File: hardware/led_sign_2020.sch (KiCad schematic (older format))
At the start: 25 parts, among them U1 ESP32-DevKitC, U2 MC74VHC1GT125, U3 MC74VHC1GT125, U4 MAX17601, U5 MAX17601, U6 MAX17601, U7 MAX17601

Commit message: change enable lines to be pulled down and microcontrolled. light up when enabled.
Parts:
- removed R2, R3, R4, R5, R6, R7: 10k, symbol Device:R_Small_US
- added D? (x2): LED, LED_SMD:LED_0805_2012Metric, symbol Device:LED
- added R?: 68ohm, Resistor_SMD:R_0805_2012Metric, symbol Device:R_Small_US
- added R?: 10k, Resistor_SMD:R_0805_2012Metric, symbol Device:R_Small_US
- R1: value 10k -> 4.7k; footprint (none) -> Resistor_SMD:R_0805_2012Metric
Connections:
- wire segments 188 -> 176
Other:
- moved on the sheet: R1

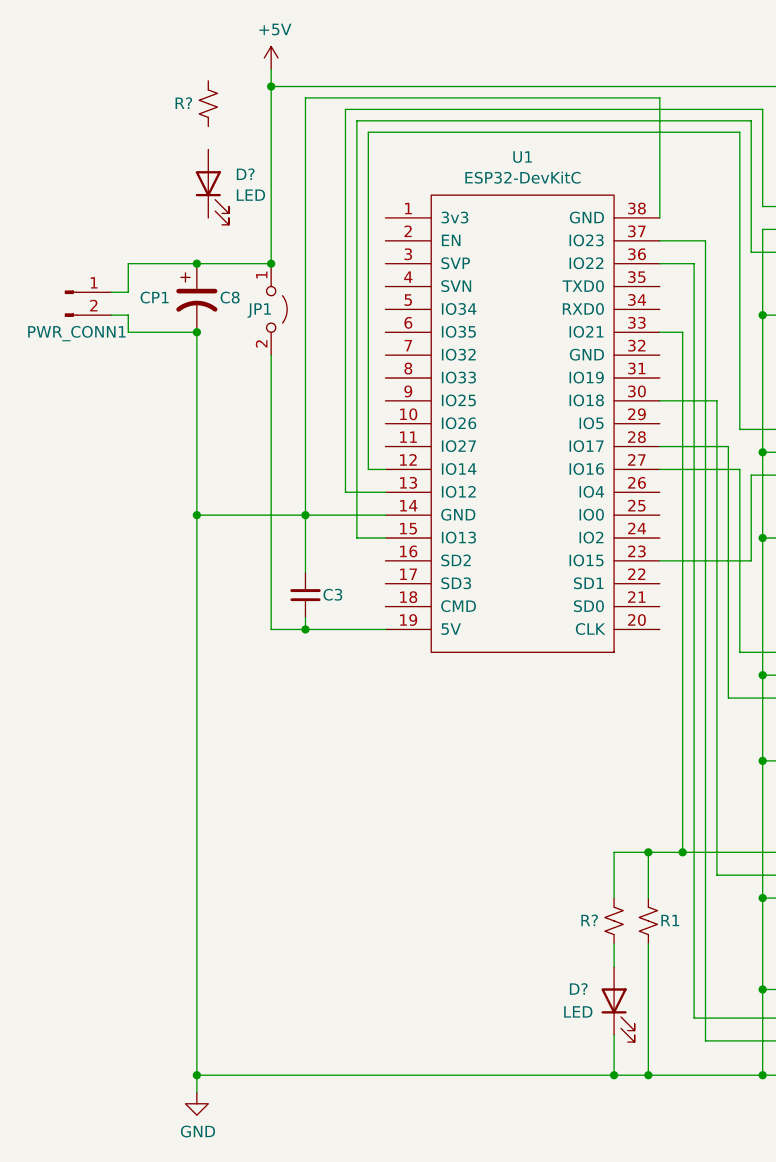
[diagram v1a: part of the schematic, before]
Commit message: add power LEDs
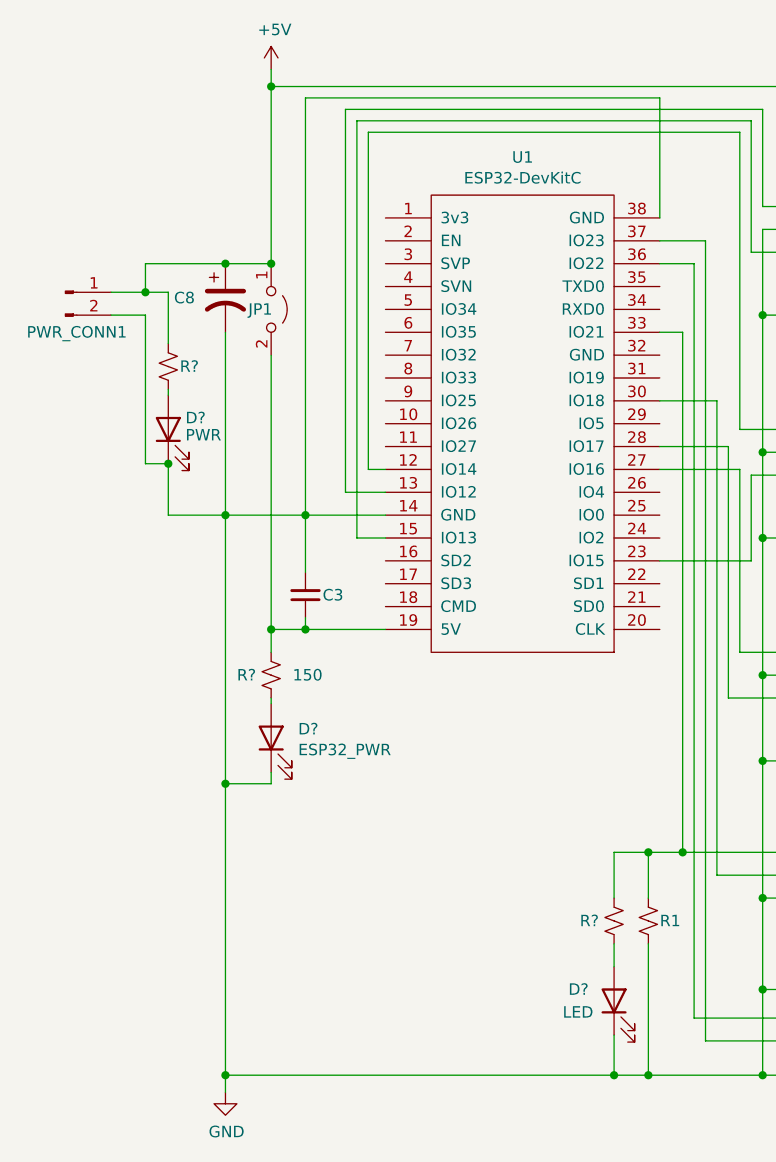
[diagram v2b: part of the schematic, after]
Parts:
- added D?: ESP32_PWR, LED_SMD:LED_0805_2012Metric, symbol Device:LED
- added R?: 150, Resistor_SMD:R_0805_2012Metric, symbol Device:R_Small_US
- D?: value LED -> PWR
- R?: value 10k -> 150
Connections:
- wire segments 176 -> 186
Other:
- moved on the sheet: C8, D?, R?

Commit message: annotate
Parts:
- gave numbers to parts that had none: 6
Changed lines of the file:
@@
 	4100 2250 4200 2250
 $Comp
-L Device:LED D?
+L Device:LED D3
 U 1 1 5FFD0A92
 P 3900 5175
-F 0 "D?" V 3950 5375 50  0000 R CNN
+F 0 "D3" V 3950 5375 50  0000 R CNN
 F 1 "LED" V 3850 5400 50  0000 R CNN
 F 2 "LED_SMD:LED_0805_2012Metric" H 3900 5175 50  0001 C CNN
@@
 $EndComp
 $Comp
-L Device:R_Small_US R?
+L Device:R_Small_US R4
 U 1 1 5FFD1F90
 P 3900 4825
-F 0 "R?" H 4050 4825 50  0000 R CNN
+F 0 "R4" H 4050 4825 50  0000 R CNN
 F 1 "68ohm" H 3968 4780 50  0001 L CNN
 F 2 "Resistor_SMD:R_0805_2012Metric" H 3900 4825 50  0001 C CNN
@@
 Connection ~ 4750 4525
 $Comp
-L Device:LED D?
+L Device:LED D1
 U 1 1 5FFF4A83
 P 1950 2675
-F 0 "D?" V 2000 2600 50  0000 R CNN
+F 0 "D1" V 2000 2600 50  0000 R CNN
 F 1 "PWR" V 1925 2600 50  0000 R CNN
 F 2 "LED_SMD:LED_0805_2012Metric" H 1950 2675 50  0001 C CNN
@@
 $EndComp
 $Comp
-L Device:R_Small_US R?
+L Device:R_Small_US R2
 U 1 1 5FFF4A89
 P 1950 2400
-F 0 "R?" H 1900 2400 50  0000 R CNN
+F 0 "R2" H 1900 2400 50  0000 R CNN
 F 1 "150" H 2018 2355 50  0001 L CNN
 F 2 "Resistor_SMD:R_0805_2012Metric" H 1950 2400 50  0001 C CNN
@@
 $EndComp
 $Comp
-L Device:LED D?
+L Device:LED D2
 U 1 1 600F026A
 P 2400 4025
-F 0 "D?" V 2439 3907 50  0000 R CNN
+F 0 "D2" V 2439 3907 50  0000 R CNN
 F 1 "ESP32_PWR" V 2348 3907 50  0000 R CNN
 F 2 "LED_SMD:LED_0805_2012Metric" H 2400 4025 50  0001 C CNN
@@
 $EndComp
 $Comp
-L Device:R_Small_US R?
+L Device:R_Small_US R3
 U 1 1 600F043E
 P 2400 3750
-F 0 "R?" H 2550 3750 50  0000 R CNN
+F 0 "R3" H 2550 3750 50  0000 R CNN
 F 1 "150" H 2175 3750 50  0000 L CNN
 F 2 "Resistor_SMD:R_0805_2012Metric" H 2400 3750 50  0001 C CNN

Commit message: assign footprints
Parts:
- JP1: footprint (none) -> Connector_PinHeader_2.54mm:PinHeader_1x02_P2.54mm_Vertical
- U2, U3: footprint (none) -> Package_SO:TSOP-5_1.65x3.05mm_P0.95mm
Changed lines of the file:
@@
 F 0 "U2" H 6800 2925 50  0000 C CNN
 F 1 "MC74VHC1GT125" H 6800 2825 50  0000 C CNN
-F 2 "" H 6800 3575 50  0001 C CNN
+F 2 "Package_SO:TSOP-5_1.65x3.05mm_P0.95mm" H 6800 3575 50  0001 C CNN
 F 3 "" H 6800 3575 50  0001 C CNN
 	1    6800 3575
@@
 F 0 "U3" H 6800 3875 50  0000 C CNN
 F 1 "MC74VHC1GT125" H 6800 3775 50  0000 C CNN
-F 2 "" H 6800 4525 50  0001 C CNN
+F 2 "Package_SO:TSOP-5_1.65x3.05mm_P0.95mm" H 6800 4525 50  0001 C CNN
 F 3 "" H 6800 4525 50  0001 C CNN
 	1    6800 4525
@@
 F 0 "JP1" V 2400 2050 50  0000 L CNN
 F 1 "Jumper_2_Open" H 2400 2294 50  0001 C CNN
-F 2 "" H 2400 2150 50  0001 C CNN
+F 2 "Connector_PinHeader_2.54mm:PinHeader_1x02_P2.54mm_Vertical" H 2400 2150 50  0001 C CNN
 F 3 "~" H 2400 2150 50  0001 C CNN
 	1    2400 2150

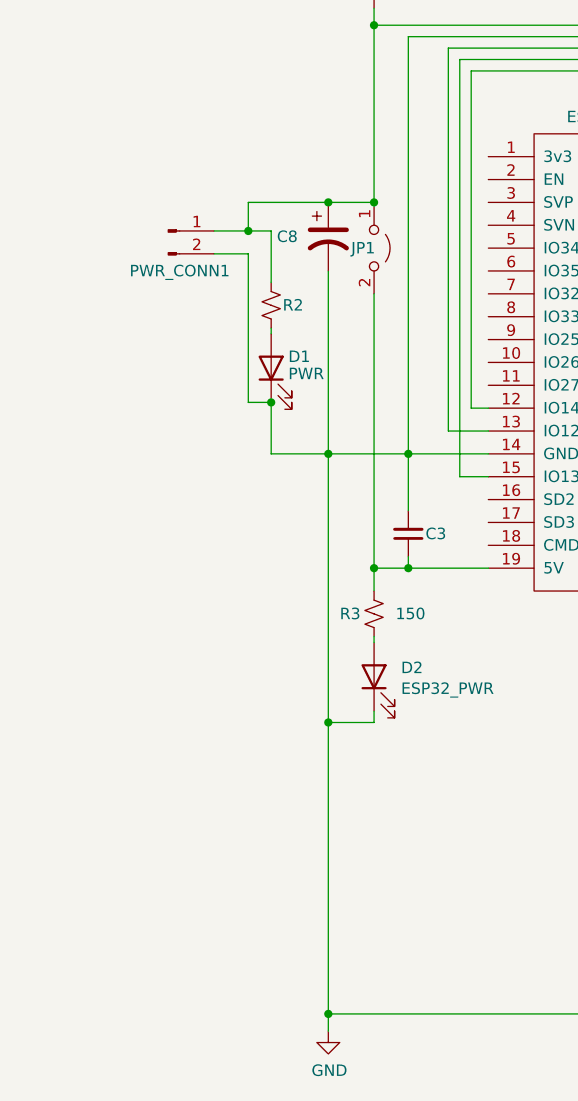
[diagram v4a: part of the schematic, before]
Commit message: add reverse polarity protection
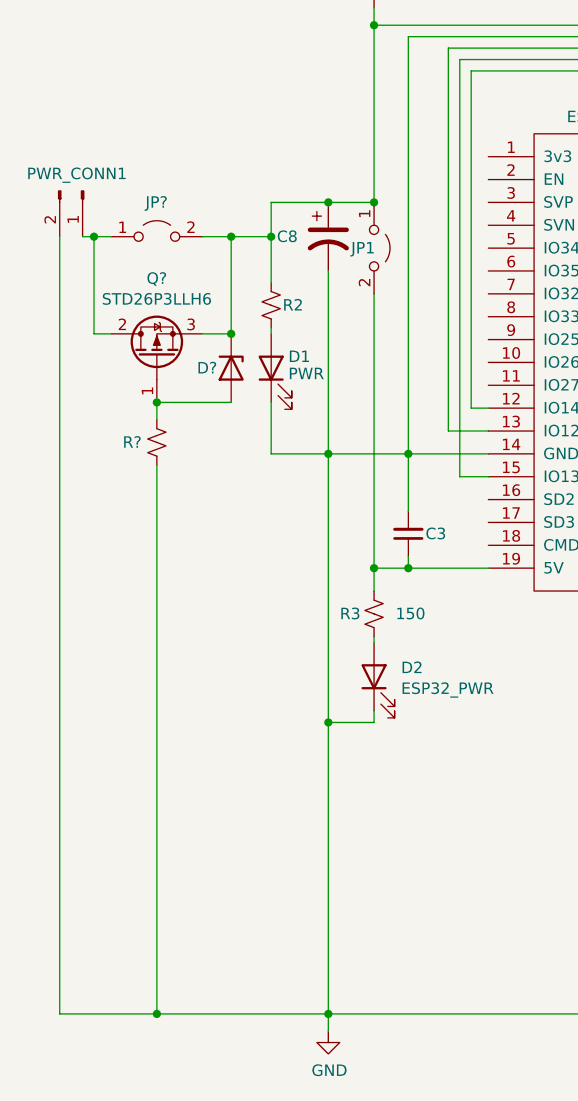
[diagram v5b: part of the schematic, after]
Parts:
- added D?: D_Zener, symbol Device:D_Zener
- added JP?: Jumper_2_Open, Connector_PinHeader_2.54mm:PinHeader_1x02_P2.54mm_Vertical, symbol Jumper:Jumper_2_Open
- added Q?: STD26P3LLH6, Package_TO_SOT_SMD:TO-252-2, symbol custom:STD26P3LLH6
- added R?: 100k, Resistor_SMD:R_0805_2012Metric, symbol Device:R_Small_US
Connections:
- wire segments 186 -> 195
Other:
- moved on the sheet: PWR_CONN1
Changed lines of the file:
@@
 L Connector:Conn_01x02_Male PWR_CONN1
 U 1 1 5FF19694
-P 1500 2075
-F 0 "PWR_CONN1" H 1550 1900 50  0000 C CNN
-F 1 "Conn_01x02_Male" H 1608 2165 50  0001 C CNN
-F 2 "" H 1500 2075 50  0001 C CNN
-F 3 "~" H 1500 2075 50  0001 C CNN
-	1    1500 2075
-	1    0    0    -1
+P 1125 1900
+F 0 "PWR_CONN1" V 1050 1875 50  0000 C CNN
+F 1 "Conn_01x02_Male" H 1233 1990 50  0001 C CNN
+F 2 "" H 1125 1900 50  0001 C CNN
+F 3 "~" H 1125 1900 50  0001 C CNN
+	1    1125 1900
+	0    1    1    0
 $EndComp
 $Comp
@@
 $EndComp
 Wire Wire Line
-	2200 1950 1850 1950
-Wire Wire Line
-	1850 1950 1850 2075
-Wire Wire Line
-	1850 2075 1950 2075
-Wire Wire Line
 	2200 2250 2200 3050
 Wire Wire Line
@@
 	3900 4525 3900 4725
 Connection ~ 4050 4525
-Connection ~ 2200 1950
 Wire Wire Line
 	1950 2500 1950 2525
@@
 	2200 3050 2550 3050
 Wire Wire Line
-	1700 2175 1850 2175
-Wire Wire Line
-	1850 2175 1850 2825
-Wire Wire Line
-	1850 2825 1950 2825
-Wire Wire Line
 	1950 2825 1950 3050
 Wire Wire Line
 	1950 3050 2200 3050
-Connection ~ 1950 2825
-Wire Wire Line
-	1950 2300 1950 2075
-Connection ~ 1850 2075
-Wire Wire Line
-	1850 2075 1700 2075
+Wire Wire Line
+	1950 2300 1950 2100
+$Comp
+L custom:STD26P3LLH6 Q?
+U 1 1 5FF8708A
+P 1450 2625
+F 0 "Q?" V 1792 2625 50  0000 C CNN
+F 1 "STD26P3LLH6" V 1701 2625 50  0000 C CNN
+F 2 "Package_TO_SOT_SMD:TO-252-2" H 1645 2550 50  0001 L CIN
+F 3 "https://www.vishay.com/docs/69253/sud19p06.pdf" H 1450 2625 50  0001 C CNN
+	1    1450 2625
+	0    -1   -1   0
+$EndComp
+$Comp
+L Device:R_Small_US R?
+U 1 1 5FF884EC
+P 1450 3000
+F 0 "R?" H 1600 3000 50  0000 R CNN
+F 1 "100k" H 1518 2955 50  0001 L CNN
+F 2 "Resistor_SMD:R_0805_2012Metric" H 1450 3000 50  0001 C CNN
+F 3 "~" H 1450 3000 50  0001 C CNN
+	1    1450 3000
+	-1   0    0    1
+$EndComp
+Wire Wire Line
+	1450 2825 1450 2900
+$Comp
+L Device:D_Zener D?
+U 1 1 5FFCF8DA
+P 1775 2675
+F 0 "D?" V 1775 2525 50  0000 L CNN
+F 1 "D_Zener" V 1820 2755 50  0001 L CNN
+F 2 "" H 1775 2675 50  0001 C CNN
+F 3 "~" H 1775 2675 50  0001 C CNN
+	1    1775 2675
+	0    1    1    0
+$EndComp
+$Comp
+L Jumper:Jumper_2_Open JP?
+U 1 1 5FFD197E
+P 1450 2100
+F 0 "JP?" H 1400 2250 50  0000 L CNN
+F 1 "Jumper_2_Open" H 1450 2244 50  0001 C CNN
+F 2 "Connector_PinHeader_2.54mm:PinHeader_1x02_P2.54mm_Vertical" H 1450 2100 50  0001 C CNN
+F 3 "~" H 1450 2100 50  0001 C CNN
+	1    1450 2100
+	1    0    0    -1
+$EndComp
+Wire Wire Line
+	1650 2525 1775 2525
+Wire Wire Line
+	1775 2825 1450 2825
+Connection ~ 1450 2825
+Wire Wire Line
+	1450 3100 1450 5500
+Wire Wire Line
+	1450 5500 2200 5500
+Wire Wire Line
+	1250 2100 1175 2100
+Wire Wire Line
+	1175 2100 1175 2525
+Wire Wire Line
+	1175 2525 1250 2525
+Wire Wire Line
+	1650 2100 1775 2100
+Wire Wire Line
+	1775 2100 1775 2525
+Connection ~ 1775 2525
+Wire Wire Line
+	1125 2100 1175 2100
+Connection ~ 1175 2100
+Wire Wire Line
+	1775 2100 1950 2100
+Connection ~ 1775 2100
+Connection ~ 1950 2100
+Wire Wire Line
+	1950 1950 2200 1950
+Wire Wire Line
+	1950 1950 1950 2100
+Connection ~ 2200 1950
+Wire Wire Line
+	1025 2100 1025 5500
+Wire Wire Line
+	1025 5500 1450 5500
+Connection ~ 1450 5500
 $EndSCHEMATC

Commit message: all kinds of reorg and netlabels
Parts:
- removed C5: 0.1uF, Capacitor_SMD:C_0805_2012Metric, symbol Device:C_Small
- added C3: 0.1uF, Capacitor_SMD:C_0805_2012Metric, symbol Device:C_Small
- Q1: renamed from Q?; footprint Package_TO_SOT_SMD:TO-252-2 -> Package_TO_SOT_SMD:TO-252-3_TabPin2
- gave numbers to parts that had none: 3
- renumbered C8 to C1, C3 to C2, C6 to C4, C7 to C5, C4 to C6, C1 to C7, C2 to C8
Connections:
- net labels added: C1, C2, C3, C4, C5, C5V, C6, C7, CCLK, CDATA, CLK, DATA, EN, R1, R2, R3, R4, R5, R6, R7
- wire segments 195 -> 134
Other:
- note added: "ESP32"
- note added: "Level Shifters"
- note added: "Power"
- note added: "Row Drivers"
- note added: "Sign Connector"
- moved on the sheet: C1, C2, C4, C5, C6, C7, C8, CONN1, D1, D2, D3, D4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

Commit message: associate footprint
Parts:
- D4: footprint (none) -> Diode_SMD:D_0805_2012Metric
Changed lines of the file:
@@
 F 0 "D4" V 3225 2100 50  0000 L CNN
 F 1 "D_Zener" V 3270 2330 50  0001 L CNN
-F 2 "" H 3225 2250 50  0001 C CNN
+F 2 "Diode_SMD:D_0805_2012Metric" H 3225 2250 50  0001 C CNN
 F 3 "~" H 3225 2250 50  0001 C CNN
 	1    3225 2250

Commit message: routing pcb
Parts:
- C1: footprint (none) -> Capacitor_THT:CP_Radial_D10.0mm_P5.00mm
- CONN1: footprint (none) -> Connector_JST:JST_XH_B12B-XH-A_1x12_P2.50mm_Vertical
- JP1: value Jumper_2_Open -> ESP32_5V
- JP2: value Jumper_2_Open -> prot_short
- PWR_CONN1: footprint (none) -> Connector_JST:JST_XH_B2B-XH-A_1x02_P2.50mm_Vertical
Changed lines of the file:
@@
 F 0 "PWR_CONN1" V 2500 1500 50  0000 C CNN
 F 1 "Conn_01x02_Male" H 2683 1615 50  0001 C CNN
-F 2 "" H 2575 1525 50  0001 C CNN
+F 2 "Connector_JST:JST_XH_B2B-XH-A_1x02_P2.50mm_Vertical" H 2575 1525 50  0001 C CNN
 F 3 "~" H 2575 1525 50  0001 C CNN
 	1    2575 1525
@@
 F 0 "CONN1" H 7828 1021 50  0000 L CNN
 F 1 "LED_sign_connection" H 7828 930 50  0000 L CNN
-F 2 "" H 7350 1700 50  0001 C CNN
+F 2 "Connector_JST:JST_XH_B12B-XH-A_1x12_P2.50mm_Vertical" H 7350 1700 50  0001 C CNN
 F 3 "" H 7350 1700 50  0001 C CNN
 	1    7350 1700
@@
 F 0 "C1" H 3425 1875 50  0000 L CNN
 F 1 "CP1" H 3400 1875 50  0001 L CNN
-F 2 "" H 3650 1875 50  0001 C CNN
+F 2 "Capacitor_THT:CP_Radial_D10.0mm_P5.00mm" H 3650 1875 50  0001 C CNN
 F 3 "~" H 3650 1875 50  0001 C CNN
 	1    3650 1875
@@
 P 2900 1725
 F 0 "JP2" H 2850 1875 50  0000 L CNN
-F 1 "Jumper_2_Open" H 2900 1869 50  0001 C CNN
+F 1 "prot_short" H 2900 1869 50  0001 C CNN
 F 2 "Connector_PinHeader_2.54mm:PinHeader_1x02_P2.54mm_Vertical" H 2900 1725 50  0001 C CNN
 F 3 "~" H 2900 1725 50  0001 C CNN
@@
 P 3850 1925
 F 0 "JP1" V 3850 1825 50  0000 L CNN
-F 1 "Jumper_2_Open" H 3850 2069 50  0001 C CNN
+F 1 "ESP32_5V" H 3850 2069 50  0001 C CNN
 F 2 "Connector_PinHeader_2.54mm:PinHeader_1x02_P2.54mm_Vertical" H 3850 1925 50  0001 C CNN
 F 3 "~" H 3850 1925 50  0001 C CNN
